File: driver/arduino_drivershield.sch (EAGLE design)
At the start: 32 parts, among them IC1 LB1973M, IC10 LB1973M, IC11 LB1973M, IC12 74HC14D, IC2 LB1973M, IC3 74HC14D, IC4 LB1973M, IC5 LB1973M, IC6 74HC14D, IC7 LB1973M, IC8 LB1973M, IC9 74HC14D, J1 J5MM, J2 J5MM, U1 ARDUINO_SHIELDLABEL

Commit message: the formar was SIGNAL@num...
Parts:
- removed J2: J5MM, jumper:J5MM
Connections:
- net 5V renamed 5V@1
- removed net @GND2: IC12C.I, IC12D.I, IC12P.GND, IC3C.I, IC3D.I, IC3P.GND, IC6C.I, IC6D.I, IC6P.GND, IC9C.I, IC9D.I, IC9P.GND, J2.2, U1.GND@0, U1.GND@1, U1.GND@2
- removed net GNDA: C1.2, C2.2, C3.2, C4.2, C5.2, C6.2, C7.2, C8.2, IC1.GND, IC10.GND, IC11.GND, IC2.GND, IC4.GND, IC5.GND, IC7.GND, IC8.GND, J2.1
- new net GND@2: IC12C.I, IC12D.I, IC12P.GND, IC3C.I, IC3D.I, IC3P.GND, IC6C.I, IC6D.I, IC6P.GND, IC9C.I, IC9D.I, IC9P.GND, U1.GND@0, U1.GND@1, U1.GND@2
- new net GND@3: C1.2, C2.2, C3.2, C4.2, C5.2, C6.2, C7.2, C8.2, IC1.GND, IC10.GND, IC11.GND, IC2.GND, IC4.GND, IC5.GND, IC7.GND, IC8.GND
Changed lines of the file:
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@@
 <part name="GND5" library="supply1" deviceset="GNDA" device=""/>
 <part name="GND8" library="supply1" deviceset="GNDA" device=""/>
-<part name="J2" library="jumper" deviceset="J" device="5MM"/>
-<part name="GND9" library="supply1" deviceset="GNDA" device=""/>
 <part name="C1" library="rcl" deviceset="C-EU" device="C0805"/>
 <part name="C2" library="rcl" deviceset="C-EU" device="C0805"/>
@@
 <instance part="U1" gate="G$1" x="25.4" y="30.48"/>
 <instance part="JP1" gate="A" x="25.4" y="63.5"/>
-<instance part="U$1" gate="G$1" x="12.7" y="25.4" rot="R90"/>
+<instance part="U$1" gate="G$1" x="7.62" y="25.4" rot="R90"/>
 <instance part="GND1" gate="1" x="10.16" y="12.7" rot="R270"/>
 <instance part="JP2" gate="G$1" x="185.42" y="86.36" rot="R180"/>
@@
 <instance part="GND5" gate="1" x="180.34" y="53.34"/>
 <instance part="GND8" gate="1" x="180.34" y="76.2"/>
-<instance part="J2" gate="1" x="-10.16" y="17.78"/>
-<instance part="GND9" gate="1" x="-15.24" y="15.24"/>
 <instance part="C1" gate="G$1" x="73.66" y="-2.54"/>
 <instance part="C2" gate="G$1" x="73.66" y="-25.4"/>
@@
 </segment>
 </net>
-<net name="5V" class="0">
+<net name="5V@1" class="0">
 <segment>
 <pinref part="U1" gate="G$1" pin="5V"/>
 <pinref part="U$1" gate="G$1" pin="5V"/>
+<wire x1="7.62" y1="25.4" x2="12.7" y2="25.4" width="0.1524" layer="91"/>
 </segment>
 <segment>
@@
 <pinref part="J1" gate="1" pin="1"/>
 <pinref part="U$3" gate="G$1" pin="5V"/>
-</segment>
-</net>
-<net name="@GND2" class="0">
-<segment>
-<pinref part="U1" gate="G$1" pin="GND@0"/>
-<pinref part="GND1" gate="1" pin="GND"/>
-<wire x1="12.7" y1="12.7" x2="12.7" y2="15.24" width="0.1524" layer="91"/>
-<junction x="12.7" y="12.7"/>
-<pinref part="U1" gate="G$1" pin="GND@1"/>
-<pinref part="J2" gate="1" pin="2"/>
-<pinref part="U1" gate="G$1" pin="GND@2"/>
-<wire x1="-5.08" y1="17.78" x2="12.7" y2="17.78" width="0.1524" layer="91"/>
-<wire x1="12.7" y1="17.78" x2="12.7" y2="15.24" width="0.1524" layer="91"/>
-<junction x="12.7" y="17.78"/>
-<junction x="12.7" y="15.24"/>
-</segment>
-<segment>
-<pinref part="IC3" gate="P" pin="GND"/>
-<pinref part="GND10" gate="1" pin="GND"/>
-<pinref part="IC3" gate="D" pin="I"/>
-<pinref part="IC3" gate="C" pin="I"/>
-<wire x1="58.42" y1="111.76" x2="58.42" y2="121.92" width="0.1524" layer="91"/>
-<junction x="58.42" y="121.92"/>
-</segment>
-<segment>
-<pinref part="IC6" gate="P" pin="GND"/>
-<pinref part="IC6" gate="C" pin="I"/>
-<pinref part="IC6" gate="D" pin="I"/>
-<wire x1="99.06" y1="111.76" x2="99.06" y2="121.92" width="0.1524" layer="91"/>
-<pinref part="GND11" gate="1" pin="GND"/>
-<junction x="99.06" y="121.92"/>
-</segment>
-<segment>
-<pinref part="IC9" gate="P" pin="GND"/>
-<pinref part="IC9" gate="D" pin="I"/>
-<pinref part="IC9" gate="C" pin="I"/>
-<wire x1="132.08" y1="111.76" x2="132.08" y2="121.92" width="0.1524" layer="91"/>
-<pinref part="GND12" gate="1" pin="GND"/>
-<junction x="132.08" y="121.92"/>
-</segment>
-<segment>
-<pinref part="IC12" gate="P" pin="GND"/>
-<pinref part="IC12" gate="C" pin="I"/>
-<pinref part="IC12" gate="D" pin="I"/>
-<wire x1="165.1" y1="114.3" x2="165.1" y2="124.46" width="0.1524" layer="91"/>
-<pinref part="GND13" gate="1" pin="GND"/>
-<junction x="165.1" y="124.46"/>
 </segment>
 </net>
@@
 </segment>
 </net>
-<net name="GNDA" class="1">
+<net name="GND@3" class="1">
 <segment>
 <pinref part="IC10" gate="G$1" pin="GND"/>
@@
 </segment>
 <segment>
-<pinref part="J2" gate="1" pin="1"/>
-<pinref part="GND9" gate="1" pin="GNDA"/>
-</segment>
-<segment>
 <pinref part="C8" gate="G$1" pin="2"/>
 <pinref part="GND15" gate="1" pin="GNDA"/>
@@
 </segment>
 </net>
+<net name="GND@2" class="0">
+<segment>
+<pinref part="U1" gate="G$1" pin="GND@0"/>
+<pinref part="GND1" gate="1" pin="GND"/>
+<wire x1="12.7" y1="12.7" x2="12.7" y2="15.24" width="0.1524" layer="91"/>
+<junction x="12.7" y="12.7"/>
+<pinref part="U1" gate="G$1" pin="GND@1"/>
+<pinref part="U1" gate="G$1" pin="GND@2"/>
+<wire x1="-5.08" y1="17.78" x2="12.7" y2="17.78" width="0.1524" layer="91"/>
+<wire x1="12.7" y1="17.78" x2="12.7" y2="15.24" width="0.1524" layer="91"/>
+<junction x="12.7" y="17.78"/>
+<junction x="12.7" y="15.24"/>
+</segment>
+<segment>
+<pinref part="IC3" gate="P" pin="GND"/>
+<pinref part="GND10" gate="1" pin="GND"/>
+<pinref part="IC3" gate="D" pin="I"/>
+<pinref part="IC3" gate="C" pin="I"/>
+<wire x1="58.42" y1="111.76" x2="58.42" y2="121.92" width="0.1524" layer="91"/>
+<junction x="58.42" y="121.92"/>
+</segment>
+<segment>
+<pinref part="IC6" gate="P" pin="GND"/>
+<pinref part="IC6" gate="C" pin="I"/>
+<pinref part="IC6" gate="D" pin="I"/>
+<wire x1="99.06" y1="111.76" x2="99.06" y2="121.92" width="0.1524" layer="91"/>
+<pinref part="GND11" gate="1" pin="GND"/>
+<junction x="99.06" y="121.92"/>
+</segment>
+<segment>
+<pinref part="IC9" gate="P" pin="GND"/>
+<pinref part="IC9" gate="D" pin="I"/>
+<pinref part="IC9" gate="C" pin="I"/>
+<wire x1="132.08" y1="111.76" x2="132.08" y2="121.92" width="0.1524" layer="91"/>
+<pinref part="GND12" gate="1" pin="GND"/>
+<junction x="132.08" y="121.92"/>
+</segment>
+<segment>
+<pinref part="IC12" gate="P" pin="GND"/>
+<pinref part="IC12" gate="C" pin="I"/>
+<pinref part="IC12" gate="D" pin="I"/>
+<wire x1="165.1" y1="114.3" x2="165.1" y2="124.46" width="0.1524" layer="91"/>
+<pinref part="GND13" gate="1" pin="GND"/>
+<junction x="165.1" y="124.46"/>
+</segment>
+</net>

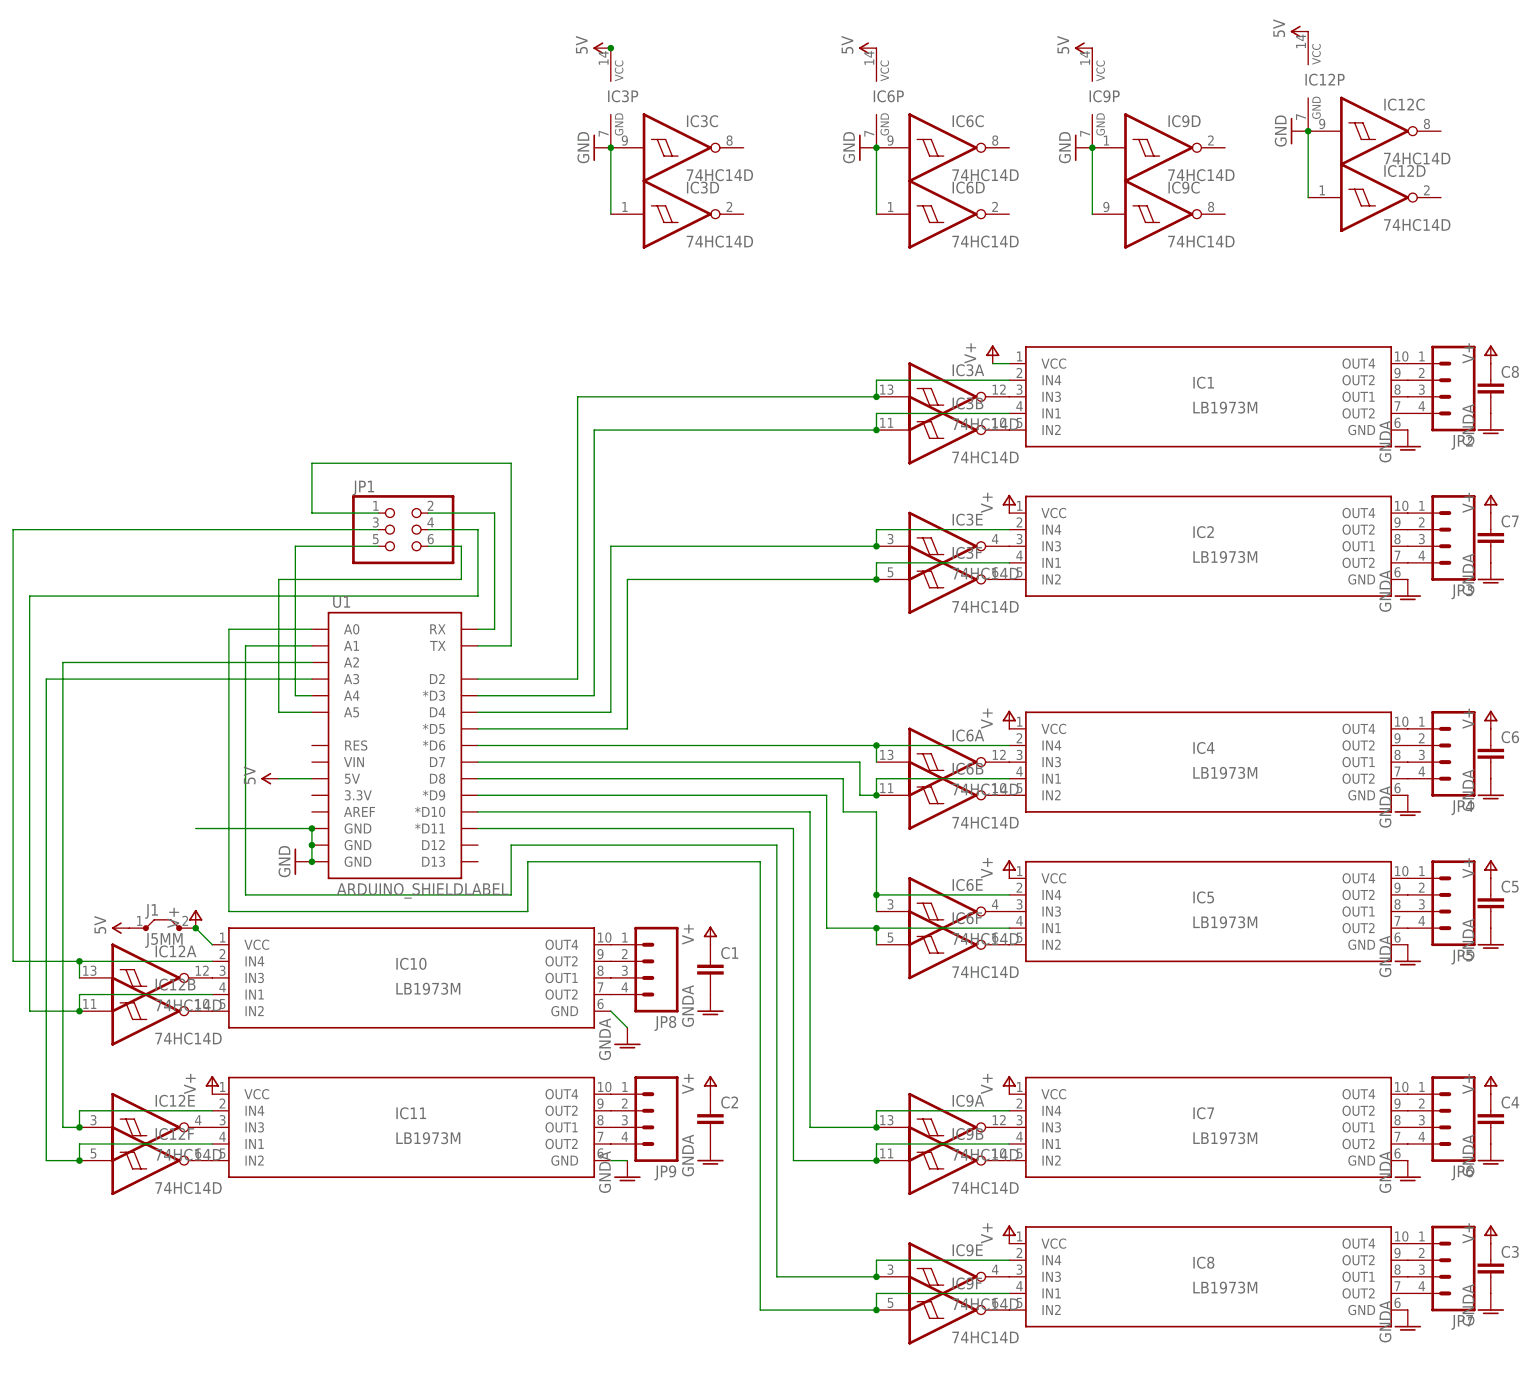
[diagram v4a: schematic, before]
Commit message: but it seems it only works in IC definitions :(
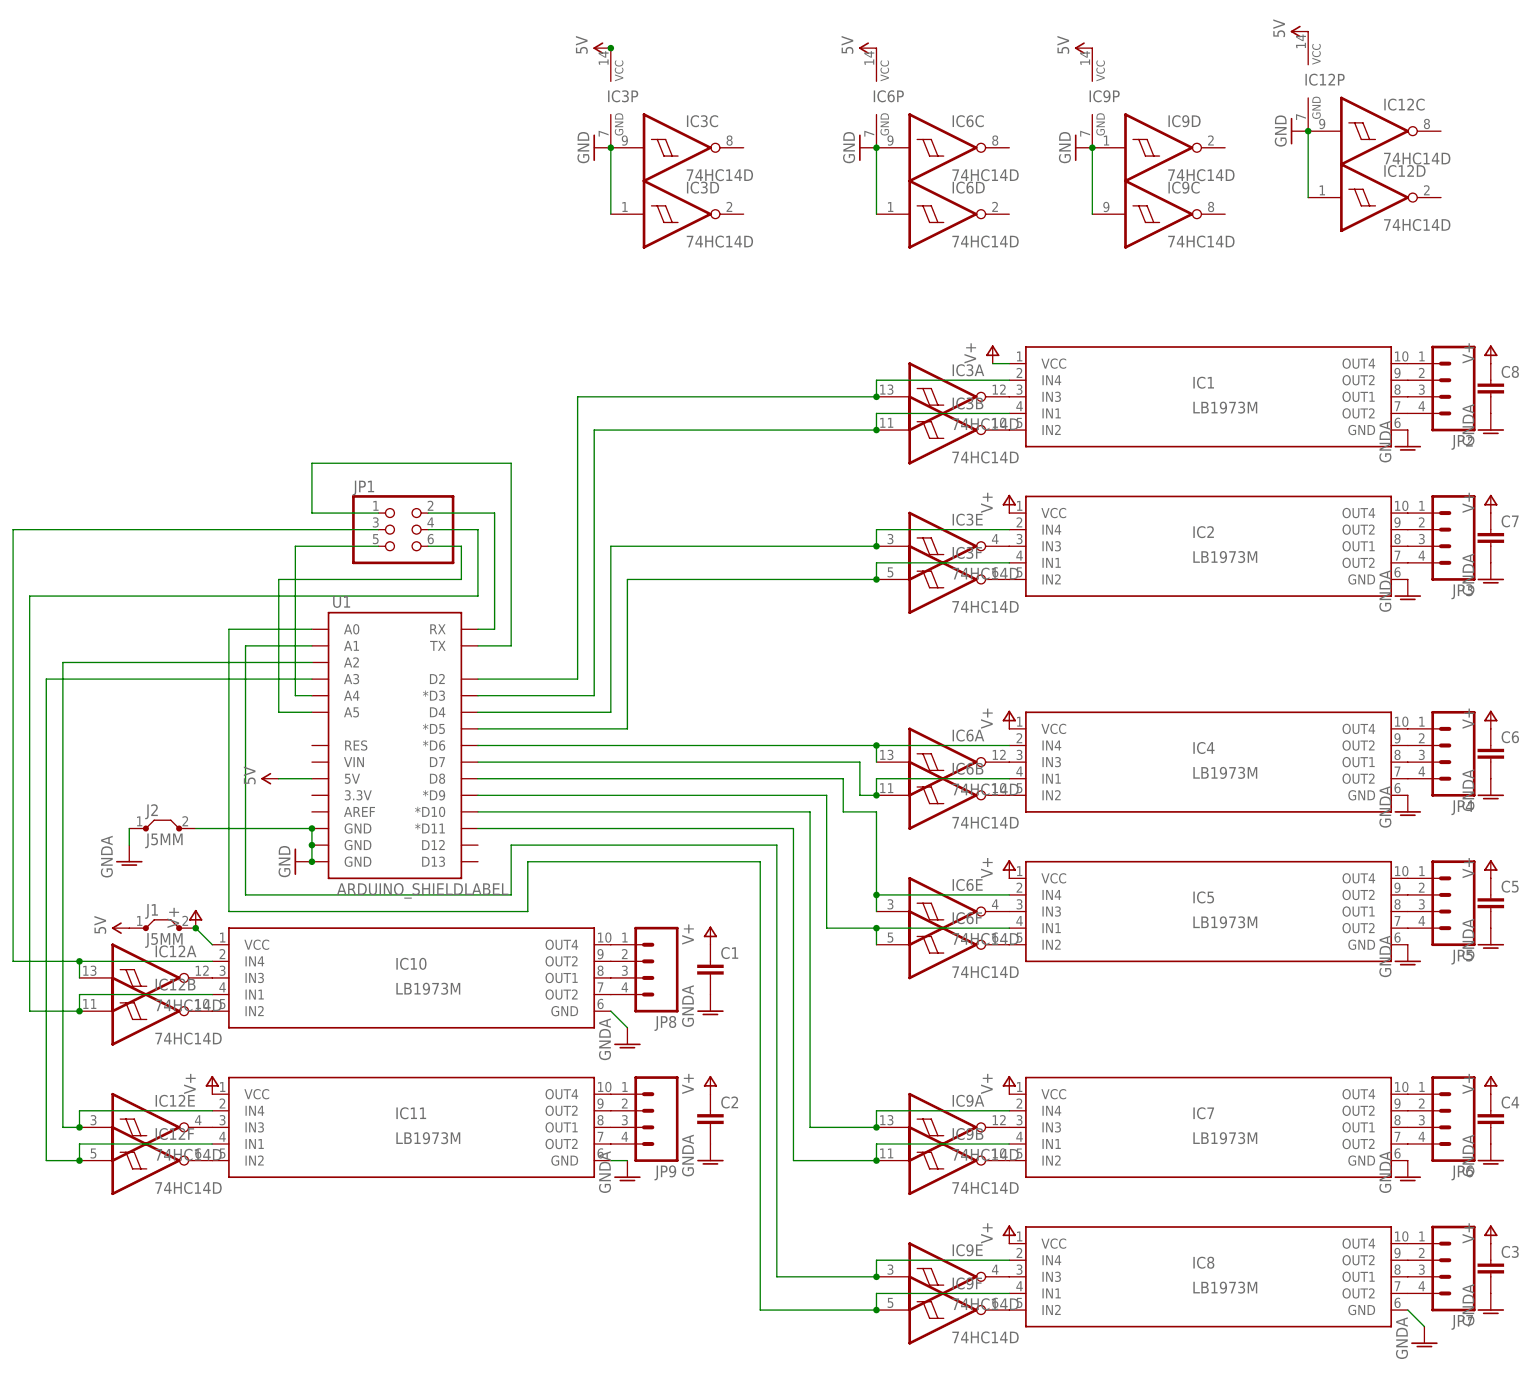
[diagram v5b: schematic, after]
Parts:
- added J2: J5MM, jumper:J5MM
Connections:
- net GND@2: now also J2.2
- net GND@3: now also J2.1
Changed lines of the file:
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@@
 <part name="P+15" library="supply1" deviceset="V+" device=""/>
 <part name="P+16" library="supply1" deviceset="V+" device=""/>
+<part name="J2" library="jumper" deviceset="J" device="5MM"/>
+<part name="GND9" library="supply1" deviceset="GNDA" device=""/>
 </parts>
 <sheets>
@@
 <instance part="GND14" gate="1" x="60.96" y="-35.56"/>
 <instance part="GND6" gate="1" x="60.96" y="-15.24"/>
-<instance part="GND7" gate="1" x="180.34" y="-58.42"/>
+<instance part="GND7" gate="1" x="182.88" y="-60.96"/>
 <instance part="GND2" gate="1" x="180.34" y="-35.56"/>
 <instance part="GND4" gate="1" x="180.34" y="-2.54"/>
@@
 <instance part="P+15" gate="1" x="73.66" y="-20.32"/>
 <instance part="P+16" gate="1" x="73.66" y="2.54"/>
+<instance part="J2" gate="1" x="-10.16" y="17.78"/>
+<instance part="GND9" gate="1" x="-15.24" y="12.7"/>
 </instances>
 <busses>
@@
 <pinref part="IC8" gate="G$1" pin="GND"/>
 <pinref part="GND7" gate="1" pin="GNDA"/>
+<wire x1="182.88" y1="-58.42" x2="180.34" y2="-55.88" width="0.1524" layer="91"/>
 </segment>
 <segment>
@@
 <wire x1="60.96" y1="-33.02" x2="58.42" y2="-33.02" width="0.1524" layer="91"/>
 <pinref part="GND14" gate="1" pin="GNDA"/>
+</segment>
+<segment>
+<pinref part="J2" gate="1" pin="1"/>
+<pinref part="GND9" gate="1" pin="GNDA"/>
+<wire x1="-15.24" y1="15.24" x2="-15.24" y2="17.78" width="0.1524" layer="91"/>
 </segment>
 </net>
@@
 <junction x="12.7" y="17.78"/>
 <junction x="12.7" y="15.24"/>
-</segment>
-<segment>
+<pinref part="J2" gate="1" pin="2"/>
+</segment>
+<segment>

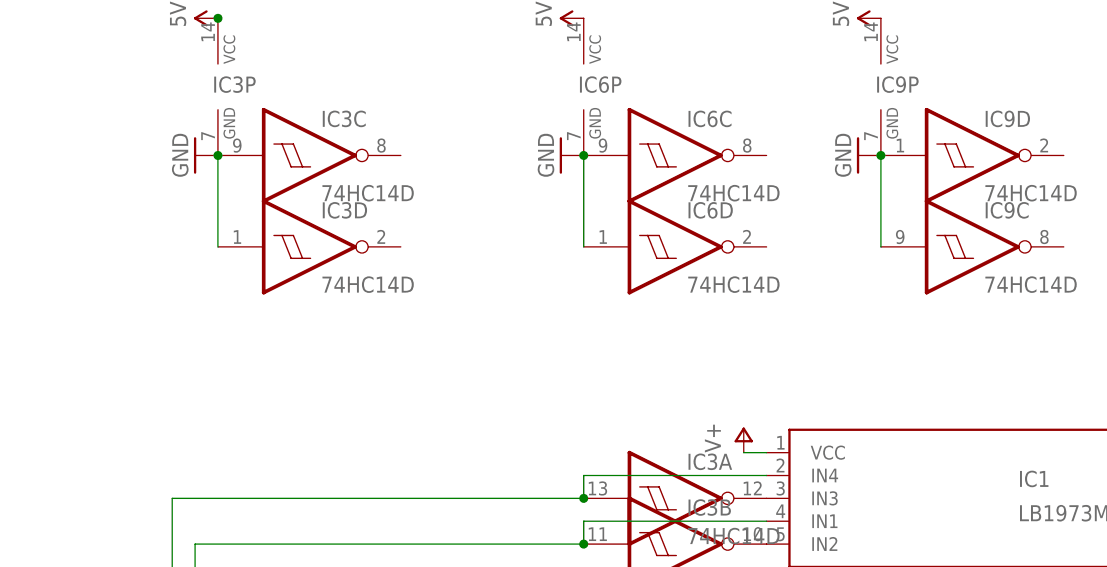
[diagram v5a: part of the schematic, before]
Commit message: add caps for the inverters too
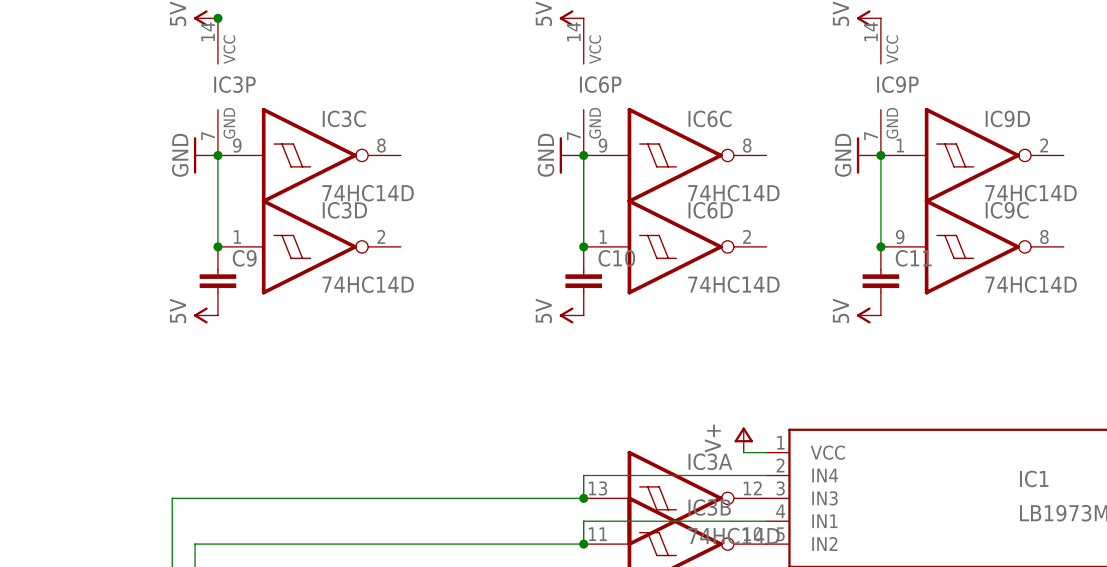
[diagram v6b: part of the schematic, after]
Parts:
- added C10, C11, C9: (no value), rcl:C-EUC0805
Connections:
- new net 5V: C10.2, C11.2, C9.2, U1.5V
- net 5V@1: no longer U1.5V
- net GND@2: now also C10.1, C11.1, C9.1
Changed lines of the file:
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@@
 <part name="J2" library="jumper" deviceset="J" device="5MM"/>
 <part name="GND9" library="supply1" deviceset="GNDA" device=""/>
+<part name="C9" library="rcl" deviceset="C-EU" device="C0805"/>
+<part name="C10" library="rcl" deviceset="C-EU" device="C0805"/>
+<part name="C11" library="rcl" deviceset="C-EU" device="C0805"/>
+<part name="U$4" library="SparkFun-Aesthetics" deviceset="5V" device=""/>
+<part name="U$5" library="SparkFun-Aesthetics" deviceset="5V" device=""/>
+<part name="U$6" library="SparkFun-Aesthetics" deviceset="5V" device=""/>
 </parts>
 <sheets>
@@
 <instance part="J2" gate="1" x="-10.16" y="17.78"/>
 <instance part="GND9" gate="1" x="-15.24" y="12.7"/>
+<instance part="C9" gate="G$1" x="58.42" y="109.22"/>
+<instance part="C10" gate="G$1" x="99.06" y="109.22"/>
+<instance part="C11" gate="G$1" x="132.08" y="109.22"/>
+<instance part="U$4" gate="G$1" x="58.42" y="104.14" rot="R90"/>
+<instance part="U$5" gate="G$1" x="99.06" y="104.14" rot="R90"/>
+<instance part="U$6" gate="G$1" x="132.08" y="104.14" rot="R90"/>
 </instances>
 <busses>
@@
 </net>
 <net name="5V@1" class="0">
-<segment>
-<pinref part="U1" gate="G$1" pin="5V"/>
-<pinref part="U$1" gate="G$1" pin="5V"/>
-<wire x1="7.62" y1="25.4" x2="12.7" y2="25.4" width="0.1524" layer="91"/>
-</segment>
 <segment>
 <pinref part="IC3" gate="P" pin="VCC"/>
@@
 <wire x1="58.42" y1="111.76" x2="58.42" y2="121.92" width="0.1524" layer="91"/>
 <junction x="58.42" y="121.92"/>
+<pinref part="C9" gate="G$1" pin="1"/>
+<junction x="58.42" y="111.76"/>
 </segment>
 <segment>
@@
 <pinref part="GND11" gate="1" pin="GND"/>
 <junction x="99.06" y="121.92"/>
+<pinref part="C10" gate="G$1" pin="1"/>
+<junction x="99.06" y="111.76"/>
 </segment>
 <segment>
@@
 <pinref part="GND12" gate="1" pin="GND"/>
 <junction x="132.08" y="121.92"/>
+<pinref part="C11" gate="G$1" pin="1"/>
+<junction x="132.08" y="111.76"/>
 </segment>
 <segment>
@@
 </segment>
 </net>
+<net name="5V" class="0">
+<segment>
+<pinref part="C9" gate="G$1" pin="2"/>
+<pinref part="U$4" gate="G$1" pin="5V"/>
+</segment>
+<segment>
+<pinref part="C10" gate="G$1" pin="2"/>
+<pinref part="U$5" gate="G$1" pin="5V"/>
+</segment>
+<segment>
+<pinref part="C11" gate="G$1" pin="2"/>
+<pinref part="U$6" gate="G$1" pin="5V"/>
+</segment>
+<segment>
+<pinref part="U1" gate="G$1" pin="5V"/>
+<pinref part="U$1" gate="G$1" pin="5V"/>
+<wire x1="7.62" y1="25.4" x2="12.7" y2="25.4" width="0.1524" layer="91"/>
+</segment>
+</net>
